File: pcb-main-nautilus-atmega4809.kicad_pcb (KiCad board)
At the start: 4 copper layers, 68.6 x 53.3 mm, 113 parts, among them J1 694106301002, J2 105017-0001, J3 FTSH-105-01-L-DV-007-K, J4 75844-101-06LF, J5 66951-006LF, J6 66951-010LF, J7 66951-008LF, J8 66951-008LF, Q1 BSS138PW, Q2 BSS138PW, Q3 BSS138PW, SW1 PTS645SH43SMTR92 LFS, U1 NCP1117-5.0_TO252, U2 AP2112K-3.3, U3 ATSAMD11D14A-SS, U4 ATmega4809-A

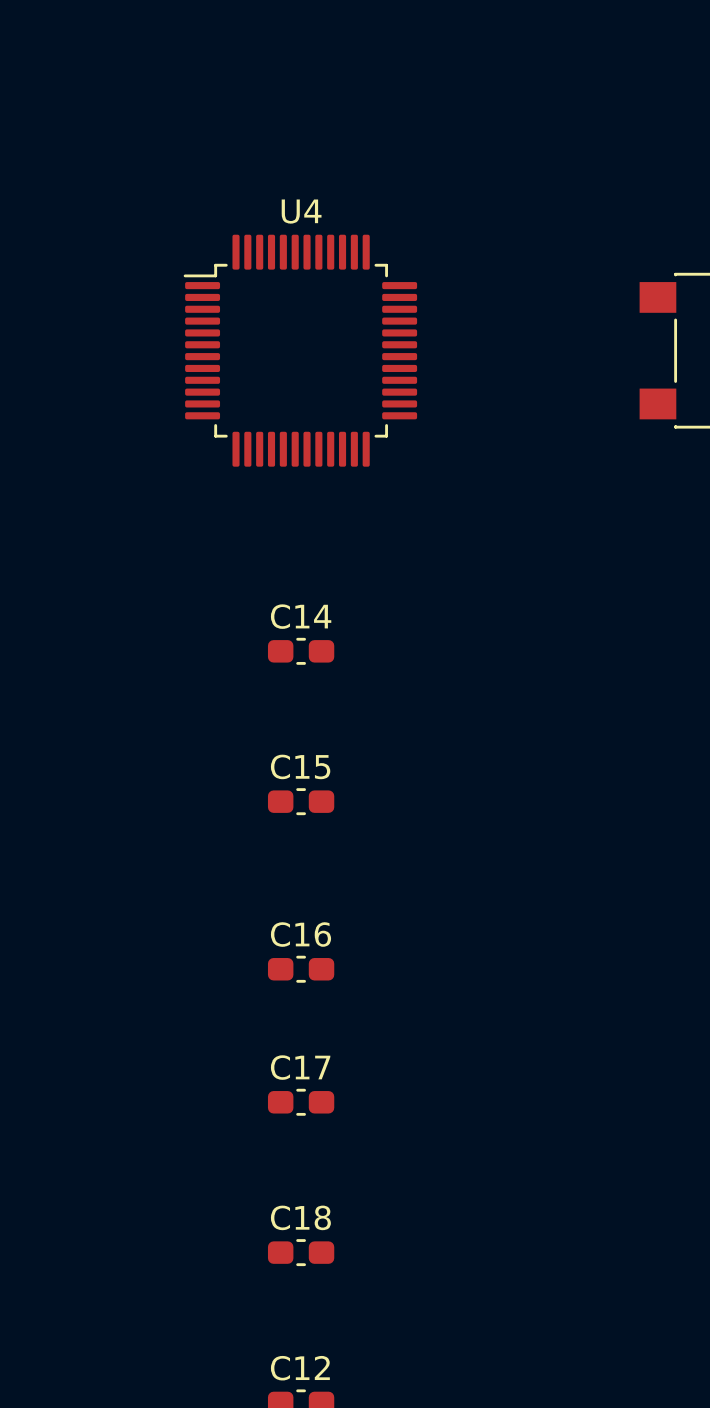
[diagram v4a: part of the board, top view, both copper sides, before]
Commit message: Arrange microcontroller decoupling capacitors
Supports #4.
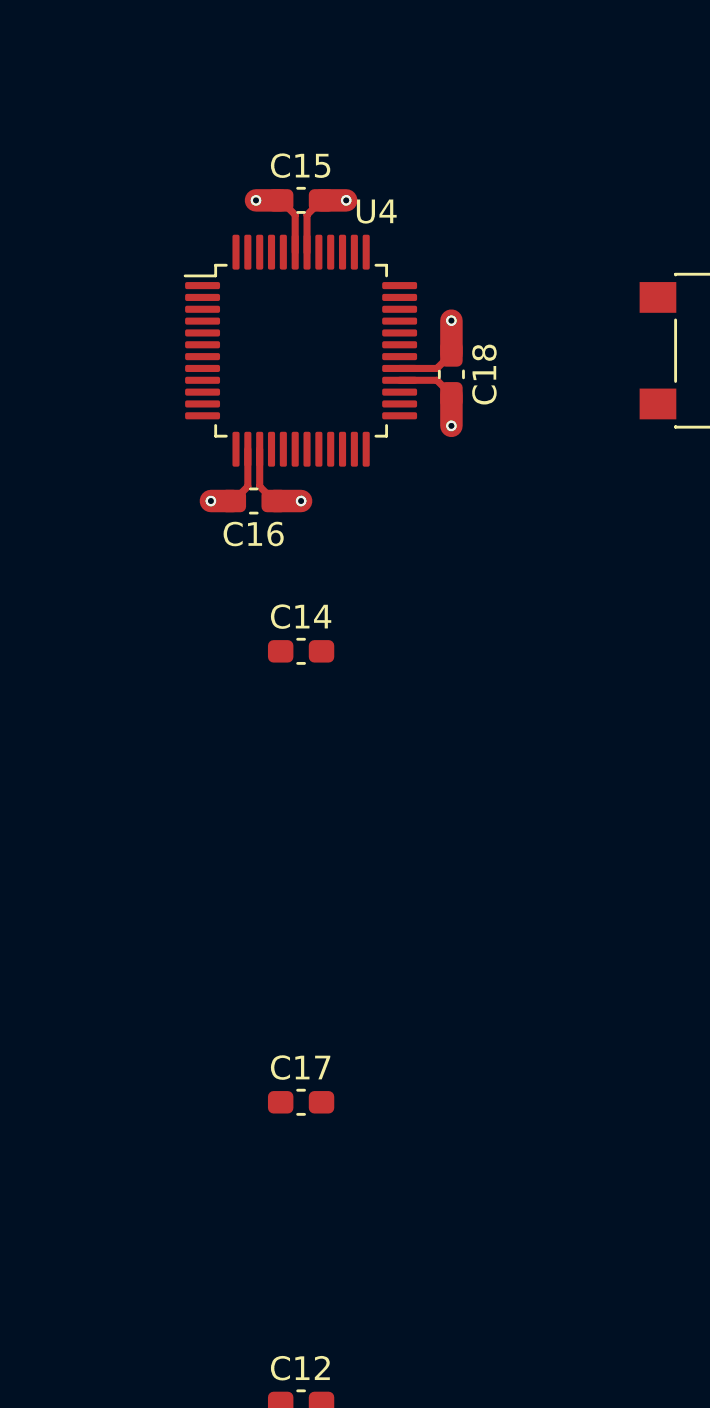
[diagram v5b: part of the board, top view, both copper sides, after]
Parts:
- moved C18 37.6 mm to (203.2, 96.2), turned to -90 degrees
- moved C15 25.4 mm to (196.8, 88.9), turned to 180 degrees
- moved C16 19.9 mm to (194.8, 101.6)
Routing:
- net /GND: track 12.8 -> 23.7 mm, vias 5 -> 8
- net /5V: track 5.18 -> 15.8 mm, vias 4 -> 7
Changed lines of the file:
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@@
     (property "Sheetname" "MCU")
     (attr smd)
-    (fp_text reference "U4" (at 0 -5.85) (layer "F.SilkS")
+    (fp_text reference "U4" (at 3.175 -5.85) (layer "F.SilkS")
       (effects (font (size 1 1) (thickness 0.15)))
     )
@@
   )
   (footprint "Capacitor_SMD:C_0603_1608Metric_Pad1.08x0.95mm_HandSolder" (layer "F.Cu")
-    (at 196.85 114.3)
+    (at 196.85 88.9 180)
     (descr "Capacitor SMD 0603 (1608 Metric), square (rectangular) end terminal, IPC_7351 nominal with elongated pad for handsoldering. (Body size source: IPC-SM-782 page 76, https://www.pcb-3d.com/wordpress/wp-content/uploads/ipc-sm-782a_amendment_1_and_2.pdf), generated with kicad-footprint-generator")
     (tags "capacitor handsolder")
@@
     (property "Sheetname" "MCU")
     (attr smd)
-    (fp_text reference "C15" (at 0 -1.43) (layer "F.SilkS")
+    (fp_text reference "C15" (at 0 1.43) (layer "F.SilkS")
       (effects (font (size 1 1) (thickness 0.15)))
     )
@@
     (fp_line (start -0.8 -0.4) (end 0.8 -0.4) (layer "F.Fab") (width 0.1))
     (fp_line (start 0.8 -0.4) (end 0.8 0.4) (layer "F.Fab") (width 0.1))
-    (pad "1" smd roundrect (at -0.8625 0) (size 1.075 0.95) (layers "F.Cu" "F.Paste" "F.Mask") (roundrect_rratio 0.25)
+    (pad "1" smd roundrect (at -0.8625 0 180) (size 1.075 0.95) (layers "F.Cu" "F.Paste" "F.Mask") (roundrect_rratio 0.25)
       (net 4 "/5V") (pintype "passive"))
-    (pad "2" smd roundrect (at 0.8625 0) (size 1.075 0.95) (layers "F.Cu" "F.Paste" "F.Mask") (roundrect_rratio 0.25)
+    (pad "2" smd roundrect (at 0.8625 0 180) (size 1.075 0.95) (layers "F.Cu" "F.Paste" "F.Mask") (roundrect_rratio 0.25)
       (net 2 "/GND") (pintype "passive"))
     (model "${KICAD6_3DMODEL_DIR}/Capacitor_SMD.3dshapes/C_0603_1608Metric.wrl"
@@
   )
   (footprint "Capacitor_SMD:C_0603_1608Metric_Pad1.08x0.95mm_HandSolder" (layer "F.Cu")
-    (at 196.85 121.38)
+    (at 194.85 101.6)
     (descr "Capacitor SMD 0603 (1608 Metric), square (rectangular) end terminal, IPC_7351 nominal with elongated pad for handsoldering. (Body size source: IPC-SM-782 page 76, https://www.pcb-3d.com/wordpress/wp-content/uploads/ipc-sm-782a_amendment_1_and_2.pdf), generated with kicad-footprint-generator")
     (tags "capacitor handsolder")
@@
     (property "Sheetname" "MCU")
     (attr smd)
-    (fp_text reference "C16" (at 0 -1.43) (layer "F.SilkS")
+    (fp_text reference "C16" (at 0 1.43) (layer "F.SilkS")
       (effects (font (size 1 1) (thickness 0.15)))
     )
@@
   )
   (footprint "Capacitor_SMD:C_0603_1608Metric_Pad1.08x0.95mm_HandSolder" (layer "F.Cu")
-    (at 196.85 133.35)
+    (at 203.2 96.25 -90)
     (descr "Capacitor SMD 0603 (1608 Metric), square (rectangular) end terminal, IPC_7351 nominal with elongated pad for handsoldering. (Body size source: IPC-SM-782 page 76, https://www.pcb-3d.com/wordpress/wp-content/uploads/ipc-sm-782a_amendment_1_and_2.pdf), generated with kicad-footprint-generator")
     (tags "capacitor handsolder")
@@
     (property "Sheetname" "MCU")
     (attr smd)
-    (fp_text reference "C18" (at 0 -1.43) (layer "F.SilkS")
-      (effects (font (size 1 1) (thickness 0.15)))
-    )
-    (fp_text value "0.1uF/10V" (at 0 1.43) (layer "F.Fab")
-      (effects (font (size 1 1) (thickness 0.15)))
-    )
-    (fp_text user "${REFERENCE}" (at 0 0) (layer "F.Fab")
+    (fp_text reference "C18" (at 0 -1.43 90) (layer "F.SilkS")
+      (effects (font (size 1 1) (thickness 0.15)))
+    )
+    (fp_text value "0.1uF/10V" (at 0 1.43 90) (layer "F.Fab")
+      (effects (font (size 1 1) (thickness 0.15)))
+    )
+    (fp_text user "${REFERENCE}" (at 0 0 90) (layer "F.Fab")
       (effects (font (size 0.4 0.4) (thickness 0.06)))
     )
@@
     (fp_line (start 0.8 -0.4) (end 0.8 0.4) (layer "F.Fab") (width 0.1))
     (fp_line (start 0.8 0.4) (end -0.8 0.4) (layer "F.Fab") (width 0.1))
-    (pad "1" smd roundrect (at -0.8625 0) (size 1.075 0.95) (layers "F.Cu" "F.Paste" "F.Mask") (roundrect_rratio 0.25)
+    (pad "1" smd roundrect (at -0.8625 0 270) (size 1.075 0.95) (layers "F.Cu" "F.Paste" "F.Mask") (roundrect_rratio 0.25)
       (net 2 "/GND") (pintype "passive"))
-    (pad "2" smd roundrect (at 0.8625 0) (size 1.075 0.95) (layers "F.Cu" "F.Paste" "F.Mask") (roundrect_rratio 0.25)
+    (pad "2" smd roundrect (at 0.8625 0 270) (size 1.075 0.95) (layers "F.Cu" "F.Paste" "F.Mask") (roundrect_rratio 0.25)
       (net 4 "/5V") (pintype "passive"))
     (model "${KICAD6_3DMODEL_DIR}/Capacitor_SMD.3dshapes/C_0603_1608Metric.wrl"
@@
   (gr_line locked (start 168.58 144.92) (end 168.58 112.154) (layer "Edge.Cuts") (width 0.254))
   (gr_arc locked (start 100 97.66) (mid 100.292893 96.952893) (end 101 96.66) (layer "Edge.Cuts") (width 0.254))
+  (segment (start 196.6 91.0875) (end 196.6 89.5125) (width 0.3) (layer "F.Cu") (net 2))
+  (segment (start 196.6 89.5125) (end 195.9875 88.9) (width 0.3) (layer "F.Cu") (net 2))
+  (segment (start 195.9875 88.9) (end 194.945 88.9) (width 0.95) (layer "F.Cu") (net 2))
   (segment (start 142.24 75.565) (end 142.24 74.93) (width 0.75) (layer "F.Cu") (net 2))
   (segment (start 142.24 74.295) (end 144.04 74.295) (width 0.75) (layer "F.Cu") (net 2))
   (segment (start 133.7575 69.215) (end 133.985 69.4425) (width 0.127) (layer "F.Cu") (net 2))
+  (segment (start 203.2 95.3875) (end 203.2 93.98) (width 0.95) (layer "F.Cu") (net 2))
   (segment (start 135.89 79.83) (end 136.98 79.83) (width 0.95) (layer "F.Cu") (net 2))
+  (segment (start 195.1 100.9875) (end 195.7125 101.6) (width 0.3) (layer "F.Cu") (net 2))
+  (segment (start 195.1 99.4125) (end 195.1 100.9875) (width 0.3) (layer "F.Cu") (net 2))
   (segment (start 110.49 74.93) (end 109.22 74.93) (width 0.95) (layer "F.Cu") (net 2))
   (segment (start 144.04 75.565) (end 142.24 75.565) (width 0.75) (layer "F.Cu") (net 2))
@@
   (segment (start 115.57 78.74) (end 114.3 78.74) (width 1) (layer "F.Cu") (net 2))
   (segment (start 111.5325 74.93) (end 110.49 74.93) (width 0.95) (layer "F.Cu") (net 2))
+  (segment (start 201.0125 96) (end 202.5875 96) (width 0.3) (layer "F.Cu") (net 2))
+  (segment (start 202.5875 96) (end 203.2 95.3875) (width 0.3) (layer "F.Cu") (net 2))
+  (segment (start 195.7125 101.6) (end 196.85 101.6) (width 0.95) (layer "F.Cu") (net 2))
   (segment (start 133.985 69.4425) (end 134.8475 69.4425) (width 0.95) (layer "F.Cu") (net 2))
   (segment (start 131.65 69.215) (end 133.7575 69.215) (width 0.6) (layer "F.Cu") (net 2))
   (via (at 134.8475 69.4425) (size 0.4572) (drill 0.254) (layers "F.Cu" "B.Cu") (net 2))
+  (via (at 203.2 93.98) (size 0.4572) (drill 0.254) (layers "F.Cu" "B.Cu") (net 2))
   (via (at 142.24 74.93) (size 0.4572) (drill 0.254) (layers "F.Cu" "B.Cu") (net 2))
   (via (at 110.49 74.93) (size 0.4572) (drill 0.254) (layers "F.Cu" "B.Cu") (net 2))
   (via (at 136.98 79.83) (size 0.4572) (drill 0.254) (layers "F.Cu" "B.Cu") (net 2))
+  (via (at 194.945 88.9) (size 0.4572) (drill 0.254) (layers "F.Cu" "B.Cu") (net 2))
+  (via (at 196.85 101.6) (size 0.4572) (drill 0.254) (layers "F.Cu" "B.Cu") (net 2))
   (via (at 114.3 78.74) (size 0.4572) (drill 0.254) (layers "F.Cu" "B.Cu") (net 2))
+  (segment (start 194.6 100.9875) (end 193.9875 101.6) (width 0.3) (layer "F.Cu") (net 4))
   (segment (start 109.22 78.74) (end 110.49 78.74) (width 1) (layer "F.Cu") (net 4))
+  (segment (start 194.6 99.4125) (end 194.6 100.9875) (width 0.3) (layer "F.Cu") (net 4))
+  (segment (start 197.7125 88.9) (end 198.755 88.9) (width 0.95) (layer "F.Cu") (net 4))
+  (segment (start 193.9875 101.6) (end 193.04 101.6) (width 0.95) (layer "F.Cu") (net 4))
+  (segment (start 202.5875 96.5) (end 203.2 97.1125) (width 0.3) (layer "F.Cu") (net 4))
+  (segment (start 203.2 97.1125) (end 203.2 98.425) (width 0.95) (layer "F.Cu") (net 4))
   (segment (start 115.6825 59.77) (end 114.38 59.77) (width 0.95) (layer "F.Cu") (net 4))
+  (segment (start 197.1 89.5125) (end 197.7125 88.9) (width 0.3) (layer "F.Cu") (net 4))
+  (segment (start 201.0125 96.5) (end 202.5875 96.5) (width 0.3) (layer "F.Cu") (net 4))
   (segment (start 115.6825 55.325) (end 114.38 55.325) (width 0.95) (layer "F.Cu") (net 4))
+  (segment (start 197.1 91.0875) (end 197.1 89.5125) (width 0.3) (layer "F.Cu") (net 4))
   (segment (start 115.6825 64.215) (end 114.38 64.215) (width 0.95) (layer "F.Cu") (net 4))
+  (via (at 198.755 88.9) (size 0.4572) (drill 0.254) (layers "F.Cu" "B.Cu") (net 4))
   (via (at 114.38 64.215) (size 0.4572) (drill 0.254) (layers "F.Cu" "B.Cu") (net 4))
+  (via (at 193.04 101.6) (size 0.4572) (drill 0.254) (layers "F.Cu" "B.Cu") (net 4))
+  (via (at 203.2 98.425) (size 0.4572) (drill 0.254) (layers "F.Cu" "B.Cu") (net 4))
   (via (at 110.49 78.74) (size 0.4572) (drill 0.254) (layers "F.Cu" "B.Cu") (net 4))
   (via (at 114.38 55.325) (size 0.4572) (drill 0.254) (layers "F.Cu" "B.Cu") (net 4))

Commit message: Remove unnecessary test points
Supports #4.
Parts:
- removed the TP25 at (25.4, 63.5)
- removed the TP26 at (25.4, 69.8)
- removed the TP27 at (31.8, 63.5)
- removed the TP28 at (25.4, 76.2)
- removed the TP29 at (31.8, 69.8)
- removed the TP30 at (19.1, 63.5)
- removed the TP31 at (25.4, 82.5)
- removed the TP32 at (31.8, 76.2)
- removed the TP33 at (19.1, 69.8)
- removed TP34, TP35, TP36, TP37, TP38, TP39, TP40, TP41, TP42, TP43, TP44, TP45, TP46: TestPoint, TestPoint:TestPoint_Pad_D1.0mm
- renumbered TP47 to TP25, TP48 to TP26, TP49 to TP27, TP50 to TP28, TP51 to TP29, TP52 to TP30, TP53 to TP31, TP54 to TP32, TP55 to TP33
